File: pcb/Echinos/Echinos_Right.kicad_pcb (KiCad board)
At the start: 2 copper layers, 167.4 x 138.9 mm, 133 parts, among them J200 USB_B_Micro, J201 Conn_01x04_Socket, J203 Conn_01x06_Socket, J204 Conn_01x06_Socket, J205 Conn_01x06_Socket, J206 USB_C_Receptacle_USB2.0, J207 Conn_01x05_Socket, SW200 SW_Push, SW201 SW_Push, SW202 SW_Push, SW203 SW_Push, SW204 SW_Push, SW205 SW_Push, SW206 SW_Push, SW207 SW_Push, SW208 SW_Push, SW209 SW_Push, SW210 SW_Push, SW211 SW_Push, SW212 SW_Push, SW213 SW_Push, SW214 SW_Push, SW215 SW_Push, SW216 SW_Push, SW217 SW_Push, SW218 SW_Push, SW219 SW_Push, SW220 SW_Push, SW221 SW_Push, SW222 SW_Push, SW223 SW_Push, SW224 Boot, SW225 Boot, SW226 Reset, SW227 Reset, U200 W25Q128JVP, U201 RP2040, U202 USBLC6-2P6, U203 74LVC1T45, U204 USBLC6-2P6, U205 XC6210B332MR-G, Y200 Crystal_GND24

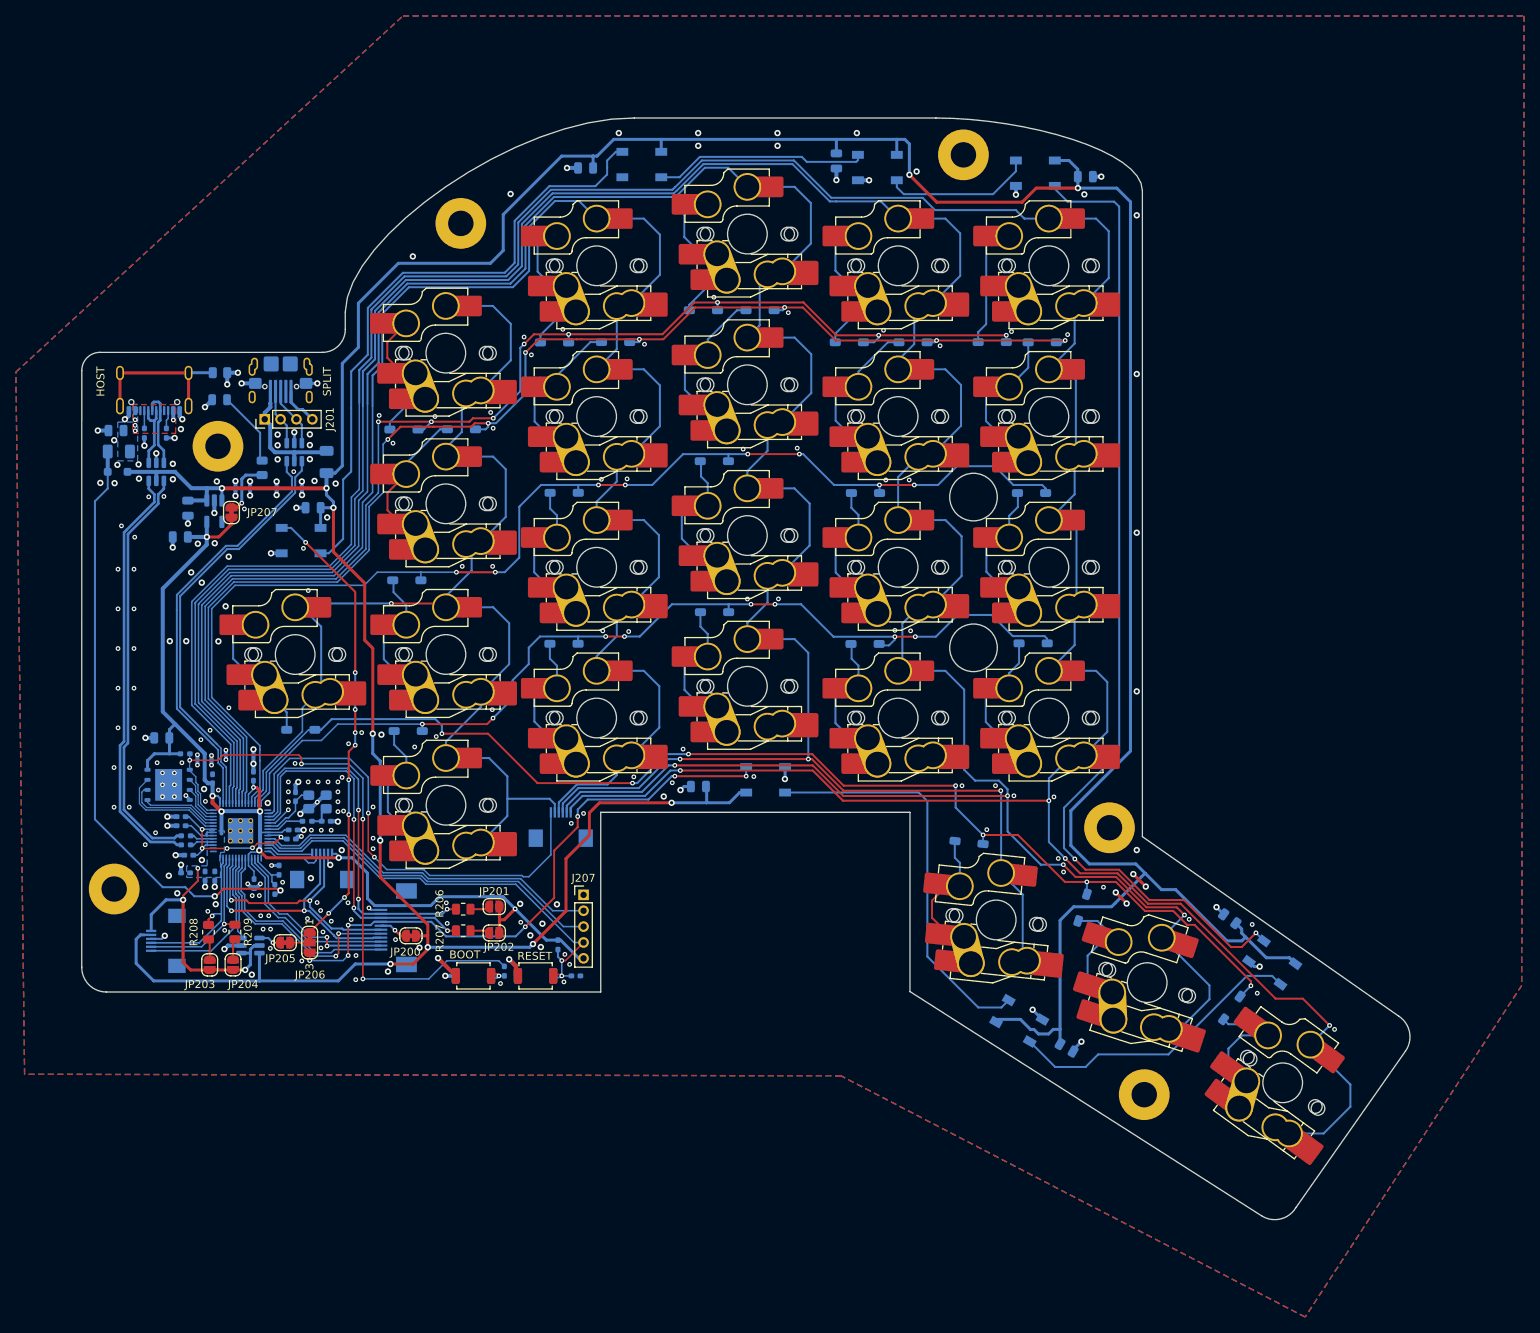
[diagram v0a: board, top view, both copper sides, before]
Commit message: [PCB] - Save last state with on board RP2040.   - Fix flash component orientation for JLCPCB assembly   - Add logo + version   - Add TH in flash footprint and use the same zone fill method as for RP2040 footprint   - Improve ground planes under switches (right side)   - Move unused schematics to backup folder (will be used to create keyboard modules later)   - Add manufacturer and part name (mfr)   - Mark optional parts as DNP   - Resync with official RP2040 symbol and update pins matching
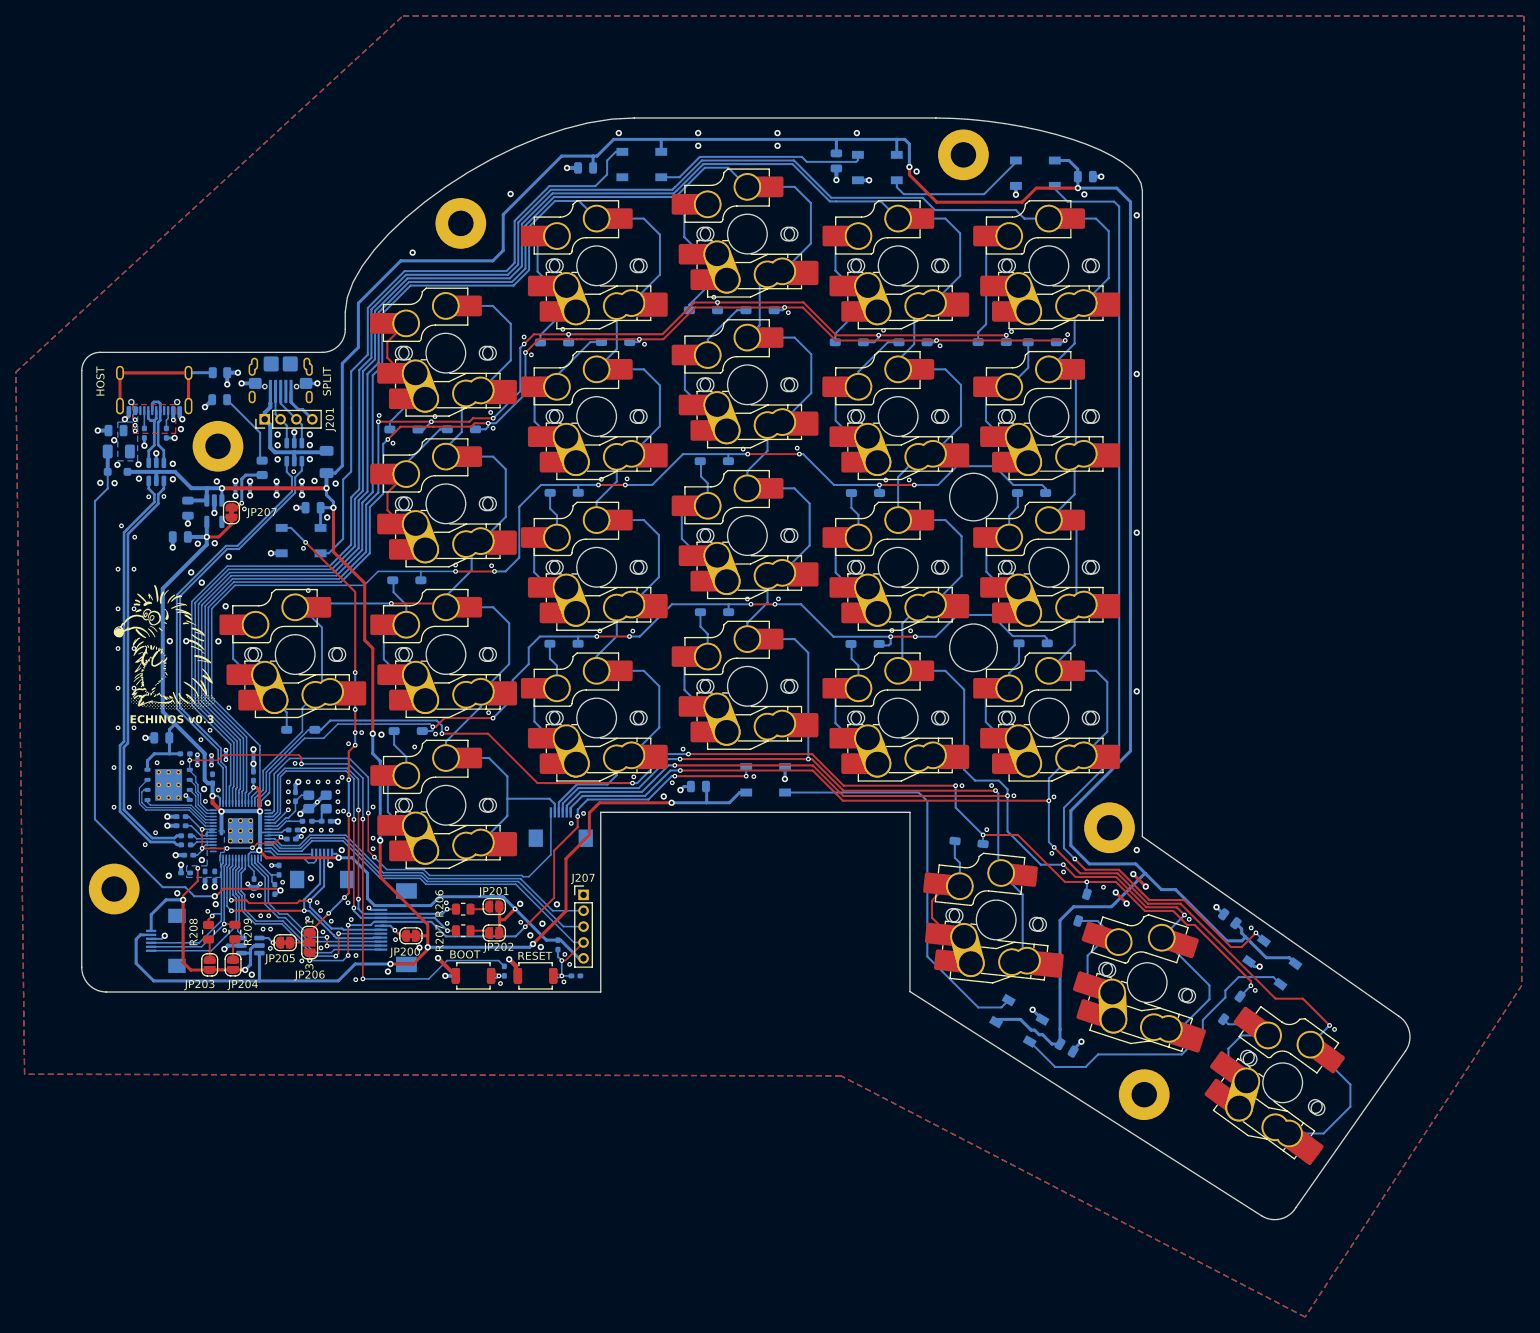
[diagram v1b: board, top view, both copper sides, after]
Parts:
- added A1: Echinos Logo, Echinos:Graphics_Hedgehog, F.Cu at (56.5, 111.8)
- H200, H201, H202, H203, H204, H205: value MountHole -> M3
- J202: value ~ -> Conn_01x12_Socket
- U200: footprint Package_SON:WSON-8-1EP_6x5mm_P1.27mm_EP3.4x4mm -> Echinos:WSON-8-1EP_6x5mm_P1.27mm_EP3.4x4mm
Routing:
- net Net-(D228-DOUT): track 38.1 -> 39.5 mm
- net row2: track 123.7 -> 124.6 mm
- net Net-(D226-DOUT): track 18.8 -> 18.2 mm
- net GND: vias 271 -> 266
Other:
- board text added: "ECHINOS v0.3"

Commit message: [PCB] - Save last state with on board RP2040.   - Move to kicad 10   - Add DRC custom rule to exclude errors on PTH for switches due to holes being too close   - Move thermal via in both RP2040 and Flash memory to pad corners (better for manufacturing)   - Update USB footprint to match changes in kicad associated symbol   - Increase trackpoint holes from 3.0 to 3.2mm (cannot do more I guess)   - Removed unused footprint from library
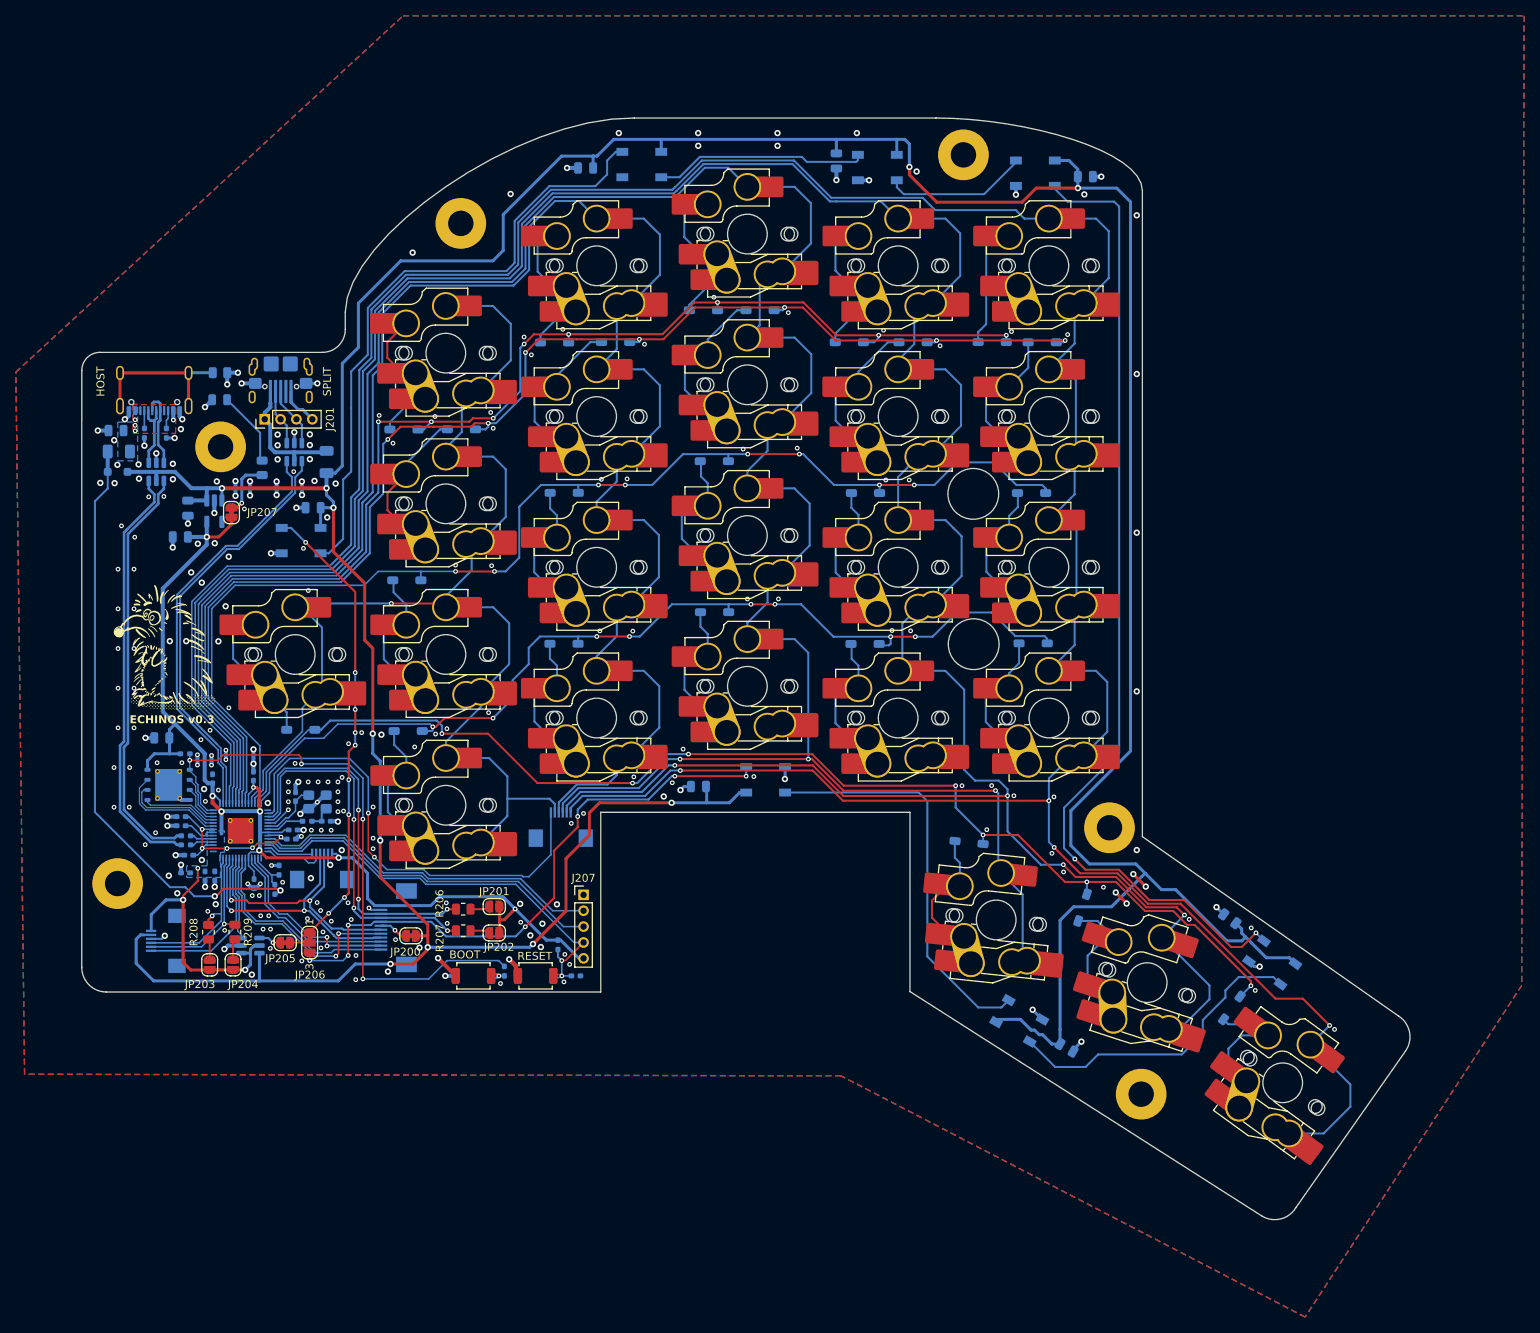
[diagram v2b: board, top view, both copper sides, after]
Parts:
- SW224, SW225: value Boot -> Button
- SW226, SW227: value Reset -> Button
- U201: footprint Echinos:RP2040-QFN-56 -> Echinos:QFN-56-1EP_7x7mm_P0.4mm_EP3.2x3.2mm_ThermalVias
- moved H203 0.81 mm to (50.6, 142.3)
- moved H201 0.39 mm to (179.6, 168.8)
- moved H204 0.34 mm to (63.6, 87.2)
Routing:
- net GND: track 99.5 -> 100.1 mm, vias 266 -> 265
- net VBUS: track 75.9 -> 75.3 mm
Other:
- outline, holes or cut-outs redrawn
